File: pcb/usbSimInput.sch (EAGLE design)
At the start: 20 parts, among them J1 PN61729-S, U1 MEGA16-P, X1 12MHz

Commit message: connected unused PORTD pins to header made board smaller
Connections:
- removed net N$10: R8.1, U1.(INT0)PD2, U1.(TXD)PD1
- removed net N$9: R7.1, U1.(RXD)PD0
- new net PD3: JP2.28, U1.(INT1)PD3
- new net PD4: JP2.29, U1.(OC1B)PD4
- new net PD5: JP2.30, U1.(OC1A)PD5
- new net PD6: JP2.31, U1.(ICP)PD6
- new net PD7: JP2.32, U1.(OC2)PD7
- net USB+: now also R7.1, R7.2, U1.(INT0)PD2, U1.(TXD)PD1; no longer R8.2
- net USB-: now also R8.1, R8.2, U1.(RXD)PD0; no longer R7.2
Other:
- moved on the sheet: R7, R8
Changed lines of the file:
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@@
 <instance part="P+6" gate="VCC" x="106.68" y="147.32"/>
 <instance part="GND22" gate="1" x="106.68" y="121.92"/>
-<instance part="R7" gate="G$1" x="182.88" y="83.82" smashed="yes">
-<attribute name="NAME" x="177.292" y="84.3026" size="1.778" layer="95"/>
-<attribute name="VALUE" x="185.42" y="84.074" size="1.778" layer="96"/>
+<instance part="R7" gate="G$1" x="33.02" y="33.02" smashed="yes" rot="R90">
+<attribute name="NAME" x="32.5374" y="27.432" size="1.778" layer="95" rot="R90"/>
+<attribute name="VALUE" x="32.766" y="35.56" size="1.778" layer="96" rot="R90"/>
 </instance>
-<instance part="R8" gate="G$1" x="182.88" y="86.36" smashed="yes">
-<attribute name="NAME" x="177.292" y="86.8426" size="1.778" layer="95"/>
-<attribute name="VALUE" x="185.42" y="86.614" size="1.778" layer="96"/>
+<instance part="R8" gate="G$1" x="40.64" y="33.02" smashed="yes" rot="R90">
+<attribute name="NAME" x="40.1574" y="27.432" size="1.778" layer="95" rot="R90"/>
+<attribute name="VALUE" x="40.386" y="35.56" size="1.778" layer="96" rot="R90"/>
 </instance>
 <instance part="D1" gate="G$1" x="33.02" y="12.7" rot="R90"/>
@@
 </instances>
 <busses>
-<bus name="PA[0..7],PB[0..7],PC[0..7]">
+<bus name="PA[0..7],PB[0..7],PC[0..7],PD[3..7]">
 <segment>
 <wire x1="172.72" y1="167.64" x2="172.72" y2="68.58" width="0.762" layer="92"/>
@@
 <net name="USB-" class="0">
 <segment>
-<pinref part="J1" gate="G$1" pin="2"/>
-<wire x1="17.78" y1="22.86" x2="25.4" y2="22.86" width="0.1524" layer="91"/>
 <pinref part="R1" gate="G$1" pin="1"/>
 <pinref part="R2" gate="G$1" pin="2"/>
+<wire x1="25.4" y1="33.02" x2="25.4" y2="22.86" width="0.1524" layer="91"/>
+<pinref part="J1" gate="G$1" pin="2"/>
+<pinref part="R8" gate="G$1" pin="1"/>
+<wire x1="25.4" y1="22.86" x2="25.4" y2="17.78" width="0.1524" layer="91"/>
+<wire x1="17.78" y1="22.86" x2="25.4" y2="22.86" width="0.1524" layer="91"/>
+<junction x="25.4" y="22.86"/>
 <wire x1="25.4" y1="22.86" x2="40.64" y2="22.86" width="0.1524" layer="91"/>
-<wire x1="40.64" y1="22.86" x2="45.72" y2="22.86" width="0.1524" layer="91"/>
-<wire x1="25.4" y1="33.02" x2="25.4" y2="22.86" width="0.1524" layer="91"/>
-<junction x="25.4" y="22.86"/>
-<wire x1="25.4" y1="22.86" x2="25.4" y2="17.78" width="0.1524" layer="91"/>
+<wire x1="40.64" y1="22.86" x2="40.64" y2="27.94" width="0.1524" layer="91"/>
+<pinref part="D2" gate="G$1" pin="C"/>
 <wire x1="40.64" y1="15.24" x2="40.64" y2="22.86" width="0.1524" layer="91"/>
 <junction x="40.64" y="22.86"/>
-<label x="43.18" y="22.86" size="1.778" layer="95"/>
-<pinref part="D2" gate="G$1" pin="C"/>
-</segment>
-<segment>
-<pinref part="R7" gate="G$1" pin="2"/>
-<wire x1="187.96" y1="83.82" x2="198.12" y2="83.82" width="0.1524" layer="91"/>
-<label x="193.04" y="83.82" size="1.778" layer="95"/>
+</segment>
+<segment>
+<pinref part="R8" gate="G$1" pin="2"/>
+<wire x1="40.64" y1="38.1" x2="40.64" y2="48.26" width="0.1524" layer="91"/>
+<label x="40.64" y="40.64" size="1.778" layer="95" rot="R90"/>
+</segment>
+<segment>
+<pinref part="U1" gate="G$1" pin="(RXD)PD0"/>
+<wire x1="157.48" y1="83.82" x2="170.18" y2="83.82" width="0.1524" layer="91"/>
+<label x="162.56" y="83.82" size="1.778" layer="95"/>
 </segment>
 </net>
@@
 <segment>
 <pinref part="J1" gate="G$1" pin="3"/>
+<pinref part="R7" gate="G$1" pin="1"/>
 <wire x1="17.78" y1="20.32" x2="33.02" y2="20.32" width="0.1524" layer="91"/>
-<wire x1="33.02" y1="20.32" x2="45.72" y2="20.32" width="0.1524" layer="91"/>
+<wire x1="33.02" y1="20.32" x2="33.02" y2="27.94" width="0.1524" layer="91"/>
+<pinref part="D1" gate="G$1" pin="C"/>
 <wire x1="33.02" y1="15.24" x2="33.02" y2="20.32" width="0.1524" layer="91"/>
 <junction x="33.02" y="20.32"/>
-<label x="43.18" y="20.32" size="1.778" layer="95"/>
-<pinref part="D1" gate="G$1" pin="C"/>
-</segment>
-<segment>
-<pinref part="R8" gate="G$1" pin="2"/>
-<wire x1="187.96" y1="86.36" x2="198.12" y2="86.36" width="0.1524" layer="91"/>
-<label x="193.04" y="86.36" size="1.778" layer="95"/>
+</segment>
+<segment>
+<pinref part="R7" gate="G$1" pin="2"/>
+<wire x1="33.02" y1="38.1" x2="33.02" y2="48.26" width="0.1524" layer="91"/>
+<label x="33.02" y="40.64" size="1.778" layer="95" rot="R90"/>
+</segment>
+<segment>
+<pinref part="U1" gate="G$1" pin="(TXD)PD1"/>
+<wire x1="157.48" y1="86.36" x2="160.02" y2="86.36" width="0.1524" layer="91"/>
+<label x="162.56" y="86.36" size="1.778" layer="95"/>
+<pinref part="U1" gate="G$1" pin="(INT0)PD2"/>
+<wire x1="160.02" y1="86.36" x2="170.18" y2="86.36" width="0.1524" layer="91"/>
+<wire x1="157.48" y1="88.9" x2="160.02" y2="88.9" width="0.1524" layer="91"/>
+<wire x1="160.02" y1="88.9" x2="160.02" y2="86.36" width="0.1524" layer="91"/>
+<junction x="160.02" y="86.36"/>
 </segment>
 </net>
@@
 </segment>
 </net>
-<net name="N$9" class="0">
-<segment>
-<pinref part="U1" gate="G$1" pin="(RXD)PD0"/>
-<pinref part="R7" gate="G$1" pin="1"/>
-<wire x1="177.8" y1="83.82" x2="157.48" y2="83.82" width="0.1524" layer="91"/>
-</segment>
-</net>
-<net name="N$10" class="0">
-<segment>
-<pinref part="U1" gate="G$1" pin="(TXD)PD1"/>
-<pinref part="R8" gate="G$1" pin="1"/>
-<wire x1="177.8" y1="86.36" x2="160.02" y2="86.36" width="0.1524" layer="91"/>
-<pinref part="U1" gate="G$1" pin="(INT0)PD2"/>
-<wire x1="160.02" y1="86.36" x2="157.48" y2="86.36" width="0.1524" layer="91"/>
-<wire x1="157.48" y1="88.9" x2="160.02" y2="88.9" width="0.1524" layer="91"/>
-<wire x1="160.02" y1="88.9" x2="160.02" y2="86.36" width="0.1524" layer="91"/>
-<junction x="160.02" y="86.36"/>
-</segment>
-</net>
 <net name="PA0" class="0">
 <segment>
@@
 </segment>
 </net>
+<net name="PD3" class="0">
+<segment>
+<pinref part="U1" gate="G$1" pin="(INT1)PD3"/>
+<wire x1="172.72" y1="88.9" x2="170.18" y2="91.44" width="0.1524" layer="91"/>
+<wire x1="170.18" y1="91.44" x2="157.48" y2="91.44" width="0.1524" layer="91"/>
+<label x="165.1" y="91.44" size="1.778" layer="95"/>
+</segment>
+<segment>
+<pinref part="JP2" gate="G$1" pin="28"/>
+<wire x1="73.66" y1="93.98" x2="71.12" y2="96.52" width="0.1524" layer="91"/>
+<wire x1="71.12" y1="96.52" x2="55.88" y2="96.52" width="0.1524" layer="91"/>
+<label x="66.04" y="96.52" size="1.778" layer="95"/>
+</segment>
+</net>
+<net name="PD4" class="0">
+<segment>
+<pinref part="U1" gate="G$1" pin="(OC1B)PD4"/>
+<wire x1="172.72" y1="91.44" x2="170.18" y2="93.98" width="0.1524" layer="91"/>
+<wire x1="170.18" y1="93.98" x2="157.48" y2="93.98" width="0.1524" layer="91"/>
+<label x="165.1" y="93.98" size="1.778" layer="95"/>
+</segment>
+<segment>
+<pinref part="JP2" gate="G$1" pin="29"/>
+<wire x1="25.4" y1="91.44" x2="27.94" y2="93.98" width="0.1524" layer="91"/>
+<wire x1="27.94" y1="93.98" x2="40.64" y2="93.98" width="0.1524" layer="91"/>
+<label x="27.94" y="93.98" size="1.778" layer="95"/>
+</segment>
+</net>
+<net name="PD5" class="0">
+<segment>
+<pinref part="U1" gate="G$1" pin="(OC1A)PD5"/>
+<wire x1="172.72" y1="93.98" x2="170.18" y2="96.52" width="0.1524" layer="91"/>
+<wire x1="170.18" y1="96.52" x2="157.48" y2="96.52" width="0.1524" layer="91"/>
+<label x="165.1" y="96.52" size="1.778" layer="95"/>
+</segment>
+<segment>
+<pinref part="JP2" gate="G$1" pin="30"/>
+<wire x1="73.66" y1="91.44" x2="71.12" y2="93.98" width="0.1524" layer="91"/>
+<wire x1="71.12" y1="93.98" x2="55.88" y2="93.98" width="0.1524" layer="91"/>
+<label x="66.04" y="93.98" size="1.778" layer="95"/>
+</segment>
+</net>
+<net name="PD6" class="0">
+<segment>
+<pinref part="U1" gate="G$1" pin="(ICP)PD6"/>
+<wire x1="172.72" y1="96.52" x2="170.18" y2="99.06" width="0.1524" layer="91"/>
+<wire x1="170.18" y1="99.06" x2="157.48" y2="99.06" width="0.1524" layer="91"/>
+<label x="165.1" y="99.06" size="1.778" layer="95"/>
+</segment>
+<segment>
+<pinref part="JP2" gate="G$1" pin="31"/>
+<wire x1="25.4" y1="88.9" x2="27.94" y2="91.44" width="0.1524" layer="91"/>
+<wire x1="27.94" y1="91.44" x2="40.64" y2="91.44" width="0.1524" layer="91"/>
+<label x="27.94" y="91.44" size="1.778" layer="95"/>
+</segment>
+</net>
+<net name="PD7" class="0">
+<segment>
+<pinref part="U1" gate="G$1" pin="(OC2)PD7"/>
+<wire x1="172.72" y1="99.06" x2="170.18" y2="101.6" width="0.1524" layer="91"/>
+<wire x1="170.18" y1="101.6" x2="157.48" y2="101.6" width="0.1524" layer="91"/>
+<label x="165.1" y="101.6" size="1.778" layer="95"/>
+</segment>
+<segment>
+<pinref part="JP2" gate="G$1" pin="32"/>
+<wire x1="73.66" y1="88.9" x2="71.12" y2="91.44" width="0.1524" layer="91"/>
+<wire x1="71.12" y1="91.44" x2="55.88" y2="91.44" width="0.1524" layer="91"/>
+<label x="66.04" y="91.44" size="1.778" layer="95"/>
+</segment>
+</net>

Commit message: pcb rev to 1.01, fixed several errors and tweaked firmware enumerates
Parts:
- added R9: 10K, resistor:R-US_0207/7
- R2: value 4K7 -> 1M
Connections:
- removed net PD3: JP2.28, U1.(INT1)PD3
- new net N$9: D1.C, J1.3, R2.1, R7.1
- new net U-RST: R1.2, U1.(INT1)PD3
- net GND: no longer JP1.3, R2.1
- net N$7: now also D2.C, J1.2, R1.1, R8.1; no longer C4.1, U1.AREF, U1.AVCC
- net RESET: now also R9.2
- net USB+: no longer D1.C, J1.3, R7.1
- net USB-: no longer D2.C, J1.2, R1.1, R2.2, R8.1
- net VCC: now also C4.1, R2.2, R9.1, U1.AREF, U1.AVCC; no longer R1.2
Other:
- moved on the sheet: D1, D2, R1, R2, R7, R8

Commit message: fixed AREF->VCC error
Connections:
- new net N$8: C4.1, U1.AREF
- net VCC: no longer C4.1, U1.AREF
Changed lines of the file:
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@@
 </segment>
 <segment>
-<pinref part="P+6" gate="VCC" pin="VCC"/>
 <pinref part="C5" gate="G$1" pin="1"/>
 <wire x1="106.68" y1="142.24" x2="106.68" y2="132.08" width="0.1524" layer="91"/>
+<pinref part="P+6" gate="VCC" pin="VCC"/>
 <wire x1="106.68" y1="144.78" x2="106.68" y2="142.24" width="0.1524" layer="91"/>
+<junction x="106.68" y="142.24"/>
 <pinref part="U1" gate="G$1" pin="VCC"/>
-<wire x1="116.84" y1="142.24" x2="106.68" y2="142.24" width="0.1524" layer="91"/>
-<junction x="106.68" y="142.24"/>
-<pinref part="C4" gate="G$1" pin="1"/>
-<pinref part="U1" gate="G$1" pin="AREF"/>
-<wire x1="91.44" y1="149.86" x2="91.44" y2="152.4" width="0.1524" layer="91"/>
-<wire x1="91.44" y1="152.4" x2="101.6" y2="152.4" width="0.1524" layer="91"/>
+<wire x1="116.84" y1="142.24" x2="111.76" y2="142.24" width="0.1524" layer="91"/>
 <pinref part="U1" gate="G$1" pin="AVCC"/>
-<wire x1="101.6" y1="152.4" x2="114.3" y2="152.4" width="0.1524" layer="91"/>
-<wire x1="114.3" y1="152.4" x2="116.84" y2="152.4" width="0.1524" layer="91"/>
-<wire x1="116.84" y1="149.86" x2="114.3" y2="149.86" width="0.1524" layer="91"/>
-<wire x1="114.3" y1="149.86" x2="114.3" y2="152.4" width="0.1524" layer="91"/>
-<junction x="114.3" y="152.4"/>
-<wire x1="106.68" y1="142.24" x2="101.6" y2="142.24" width="0.1524" layer="91"/>
-<wire x1="101.6" y1="142.24" x2="101.6" y2="152.4" width="0.1524" layer="91"/>
-<junction x="101.6" y="152.4"/>
+<wire x1="111.76" y1="142.24" x2="106.68" y2="142.24" width="0.1524" layer="91"/>
+<wire x1="116.84" y1="149.86" x2="111.76" y2="149.86" width="0.1524" layer="91"/>
+<wire x1="111.76" y1="149.86" x2="111.76" y2="142.24" width="0.1524" layer="91"/>
+<junction x="111.76" y="142.24"/>
 </segment>
 <segment>
@@
 </segment>
 </net>
+<net name="N$8" class="0">
+<segment>
+<pinref part="C4" gate="G$1" pin="1"/>
+<pinref part="U1" gate="G$1" pin="AREF"/>
+<wire x1="91.44" y1="149.86" x2="91.44" y2="152.4" width="0.1524" layer="91"/>
+<wire x1="91.44" y1="152.4" x2="116.84" y2="152.4" width="0.1524" layer="91"/>
+</segment>
+</net>

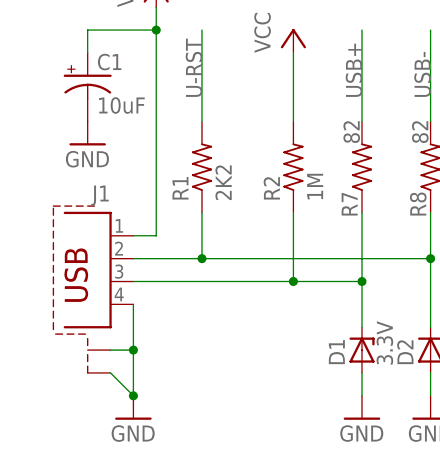
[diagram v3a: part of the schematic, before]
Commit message: edited USB connector silkscreen
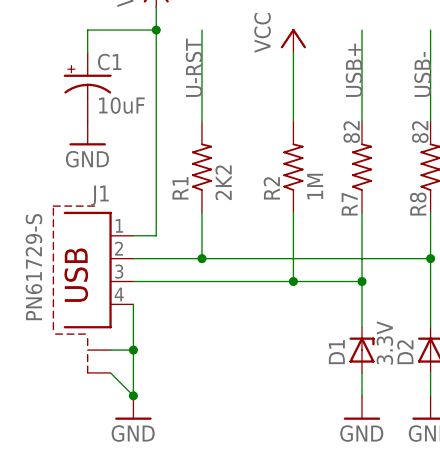
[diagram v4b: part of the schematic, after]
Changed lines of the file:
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@@
 <?xml version="1.0" encoding="utf-8"?>
 <!DOCTYPE eagle SYSTEM "eagle.dtd">
-<eagle version="6.1">
+<eagle version="7.2.0">
 <drawing>
 <settings>
@@
 <part name="FRAME1" library="frames" deviceset="LETTER_L" device=""/>
 <part name="JP1" library="con-ml" deviceset="ML10" device=""/>
-<part name="J1" library="con-berg" deviceset="PN61729-S" device="" value=""/>
+<part name="J1" library="con-berg" deviceset="PN61729-S" device="" value="PN61729-S"/>
 <part name="JP2" library="con-lstb" deviceset="MA20-2" device=""/>
 <part name="P+3" library="supply1" deviceset="VCC" device=""/>
